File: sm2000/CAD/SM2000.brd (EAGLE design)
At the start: 160 x 100 mm, 228 parts, among them CN1 HDR100-3, CN10 ST-3509, CN11 HDR100-3, CN2 JS-MU3-002, CN3 DS-0518, CN5 ST-3509, CN8 ST-3509, J1 JMP-2PIN, J2 JMP-2PIN, J3 JMP-2PIN, J4 CONN-BOOM-XH-2A, P10 TPAD50, P11 TPAD50, P12 TPAD50, P13 TPAD50, P14 TPAD50, P16 TPAD50, P18 TPAD50, P19 TPAD50, P20 TPAD50, P21 TPAD50, P3 TPAD50, P4 TPAD50, P5 TPAD50, P6 TPAD50, P7 TPAD50, P8 TPAD50, P9 TPAD50, Q1 MMBT3904, Q2 MMBT3904, Q3 MMBT3904, Q4 MMBT3904, Q5 MMBT3904, Q6 MMBT3904, Q7 BC548, Q8 BC549, SW1 SW-LC2259, SW2 TS-026, SW3 SW-LC2259EENP, SW4 TS-026, SW5 TS-02B, U1 STM32F405VGT6, U10 DNL, U2 LD3985M33R, U3 STMPS2141, U4 EMIF02-USB03F2, U5 TPS54329E, U8 LM386M-1, U9 LMV341, X1 BU-SMA-H, X2 BU-SMA-H

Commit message: Continued edit of SM2000 .sch & .brd   RGB
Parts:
- removed R55: 0 Ohm, AA-ipc-7351-resistor:RESC1608X55N
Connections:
- removed net !CPPT!: U1.57
- removed net DAC1_OUT: R55.2
- removed net N$11: R55.1, U1.29
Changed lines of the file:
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@@
 <element name="C49" library="AA-ipc-7351-capacitor" package="CAPC1005X60N" value="100nF,25V" x="-72.39" y="129.54"/>
 <element name="FB7" library="_RoweTel" package="FE0805" value="FB0805" x="-54.61" y="120.65"/>
-<element name="R55" library="AA-ipc-7351-resistor" package="RESC1608X55N" value="0 Ohm" x="-123.19" y="95.25"/>
 <element name="R54" library="AA-ipc-7351-resistor" package="RESC1608X55N" value="0 Ohm" x="-116.84" y="95.25"/>
 <element name="C55" library="AA-ipc-7351-capacitor" package="CAPC1005X60N" value="1nF,25V,0402" x="-91.44" y="129.54"/>
@@
 <wire x1="-33.37" y1="3.68" x2="-27.17" y2="106.68" width="0" layer="19" extent="1-1"/>
 </signal>
-<signal name="!CPPT!">
-<contactref element="U1" pad="57"/>
-</signal>
 <signal name="!TEST!">
 <contactref element="R4" pad="2"/>
@@
 <wire x1="-97.79" y1="10" x2="-92.24" y2="95.25" width="0" layer="19" extent="1-1"/>
 </signal>
-<signal name="DAC1_OUT">
-<contactref element="R55" pad="2"/>
-</signal>
 <signal name="DAC2_OUT">
 <contactref element="R54" pad="2"/>
@@
 <wire x1="-105.41" y1="115.57" x2="-64.3" y2="95.25" width="0" layer="19" extent="1-1"/>
 <wire x1="-116.04" y1="95.25" x2="-105.41" y2="115.57" width="0" layer="19" extent="1-1"/>
-</signal>
-<signal name="N$11">
-<contactref element="R55" pad="1"/>
-<contactref element="U1" pad="29"/>
-<wire x1="-31.62" y1="6.93" x2="-123.99" y2="95.25" width="0" layer="19" extent="1-1"/>
 </signal>
 <signal name="N$13">
@@
 </signal>
 <signal name="N$90">
+<contactref element="C76" pad="2"/>
 <contactref element="C69" pad="1"/>
-<contactref element="C76" pad="2"/>
 <contactref element="X2" pad="1"/>
 <wire x1="-91.07" y1="88.9" x2="-118.11" y2="29.21" width="0" layer="19" extent="1-1"/>

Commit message: MERGE SCHEMATICS INTO sm2000.SCH AND UPDATE LIBRARY rgb
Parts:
- added C100, C93: 33p, rcl:C025-024X044
- added C118, C121, C124, C125, C126, C129, C131, C91, C92, C97: 0.1u, rcl:C025-024X044
- added C119: 10uF, _RoweTel:C1210
- added C120: 39pF, rcl:C025-024X044
- added C122, C89: 5p6, rcl:C025-024X044
- added C123: 2-12pF, c-trimm:3008
- added C127: 27pF, rcl:C025-024X044
- added C128, C132: 150pF, rcl:C025-024X044
- added C130, C133, C134, C88, C90, C96, C98: 1n, rcl:C025-024X044
- added C87: 22pF, AA-ipc-7351-capacitor:CAPC2012X145AN
- added C94: 22p, rcl:C025-024X044
- added C95: 1n DNL, rcl:C025-024X044
- added C99: 47p, rcl:C025-024X044
- added FB11, FB14, FB15, FB6: FB0805, _RoweTel:FE0805
- added L10: 168nH, rcl:0204/5
- added L11, L13: RFC, inductor-neosid:Z15/4
- added L12: 54nH, rcl:0204/5
- added L14, L15: 57nH air core 4T 2mm ID, rcl:0204/5
- added L20: 5.7uH +/- 10% Q>20, rcl:0204/5
- added L21: 9.2uH +/- 10% Q>20, rcl:0204/5
- added L22: 5.2uH +/- 10% Q>20, rcl:0204/5
- added L23: 15uH +/- 10% Q>20, rcl:0204/5
- added L9: 57nH, rcl:0204/5
- added Q12: BRF92, transistor:SOT23-EBC
- added Q13: BFQ19, transistor:SOT23-EBC
- added Q14: RD01MUS2, _RoweTel:SOT89
- added Q17, Q18: MMT2904, transistor:SOT23-EBC
- added R108, R60, R93: 3k, AA-ipc-7351-resistor:RESC2012X70N
- added R109, R113, R94: 1k, AA-ipc-7351-resistor:RESC2012X70N
- added R110, R96, R97: 10, AA-ipc-7351-resistor:RESC2012X70N
- added R111: 33k, AA-ipc-7351-resistor:RESC2012X70N
- added R112: 15k, AA-ipc-7351-resistor:RESC2012X70N
- added R114, R95: 50, AA-ipc-7351-resistor:RESC2012X70N
- added R115, R92: 150, AA-ipc-7351-resistor:RESC2012X70N
- added R55: 10k, AA-ipc-7351-resistor:RESC2012X70N
- added R98: 47 DNL, AA-ipc-7351-resistor:RESC2012X70N
- added R99: 4k7, AA-ipc-7351-resistor:RESC2012X70N
- added U$10, U$11: ECS-10.7-15B, _RoweTel:HC49/S
- added U7: SA612A, _RoweTel:SO-08
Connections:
- new net N$11: C100.1, L14.2
- new net N$112: C87.2, L9.1
- new net N$113: C95.1, R98.1
- new net N$114: C96.1, FB11.1, R99.2
- new net N$115: C97.1, FB6.2, R99.1
- new net N$116: L13.1
- new net N$118: C93.1, C98.2, L15.1
- new net N$140: C118.1, Q17.C, R108.2, R110.2, R111.2
- new net N$141: C121.2, Q17.B, Q18.C, R108.1
- new net N$142: C119.1, FB14.1, R110.1
- new net N$143: C120.1, L20.2, U$11.1
- new net N$144: C122.1, U$10.2, U$11.2
- new net N$145: C121.1, C123.+, L21.2, U$10.1
- new net N$146: C124.1, Q18.B, R111.1, R112.2
- new net N$147: C125.1, Q18.E, R113.2
- new net N$148: C126.1, Q17.E, R109.2
- new net N$149: C126.2, C127.1, C128.2, R114.2
- new net N$150: C128.1, C129.2, L22.2, U7.2
- new net N$151: C127.2, L22.1, U7.1
- new net N$152: FB15.2, R115.2
- new net N$153: C130.2, C131.2, R115.1, U7.8
- new net N$154: C132.2, U7.6
- new net N$155: C132.1
- new net N$156: C133.2, L23.1, U7.4
- new net N$157: C134.2, L23.2
- new net N$32: C98.1, L11.1, Q14.3
- new net N$33: C94.1, FB11.2, Q14.1, R98.2
- new net N$70: C88.1, Q12.E, R92.2
- new net N$71: C90.1, Q13.E, R95.2
- new net N$73: C91.1, L10.1, R55.2, R96.2
- new net N$74: C92.1, L12.1, R93.2, R96.1, R97.2
- new net N$75: C89.1, Q13.B, R93.1, R94.2
- new net N$78: C87.1, Q12.B, R55.1, R60.2
- new net N$79: L11.2, L13.2, R97.1
- new net N$82: C89.2, L10.2, Q12.C
- new net N$84: C94.2, L12.2, Q13.C
- new net N$9: C99.1, L14.1, L15.2
- new net VGG: FB6.1
- net +12V: now also FB14.2, FB15.1
- net GND: now also C100.2, C118.2, C119.2, C120.2, C122.2, C123.-, C129.1, C131.1, C133.1, C134.1, C88.2, C90.2, C91.2, C92.2, C93.2, C95.2, C96.2, C97.2, C99.2, L21.1, L9.2, Q14.2, Q14.2.1, R109.1, R113.1, R114.1, R60.1, R92.1, R94.1, R95.1, U7.3

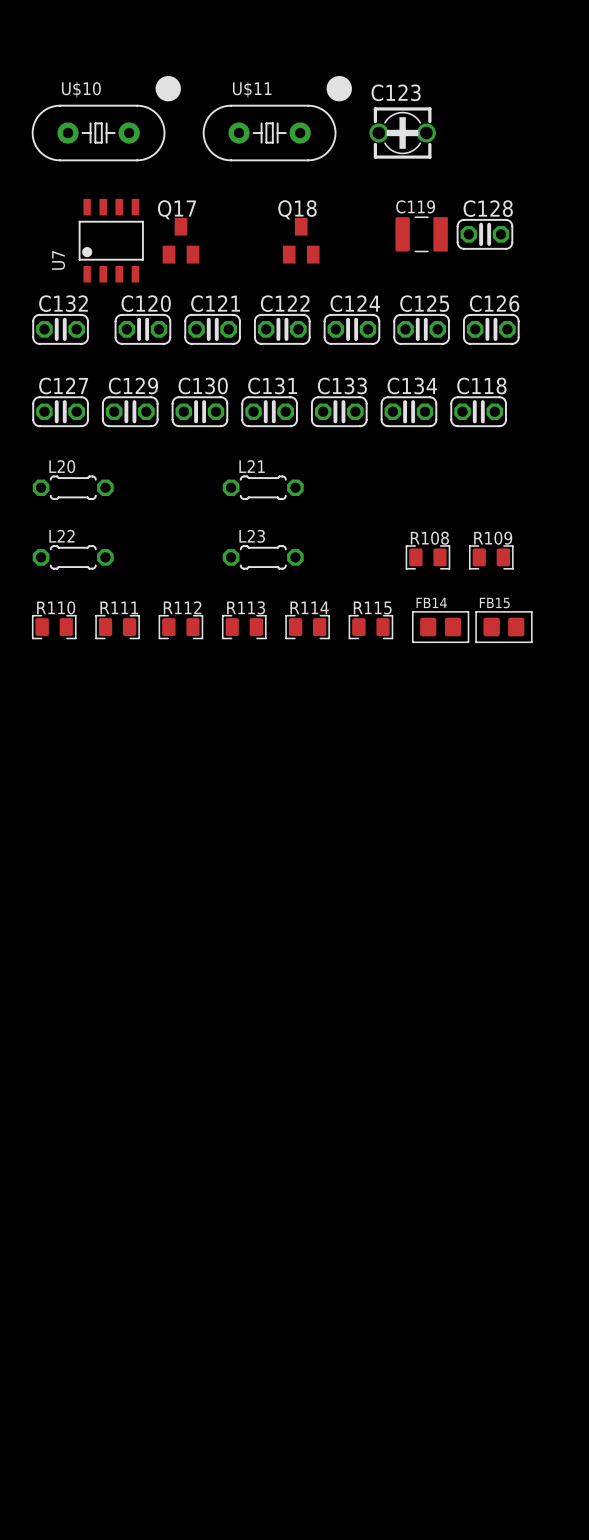
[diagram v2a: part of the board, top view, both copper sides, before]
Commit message: INTEGRATED 1ST MIXER BPF SWITCH INTO SM2000.SCH. CORRECTED CENTERING ON SOME COMPONENTS IN ROWETEL.LBR SHORTENED LEADS ON FB0805 SYMBOL. RGB
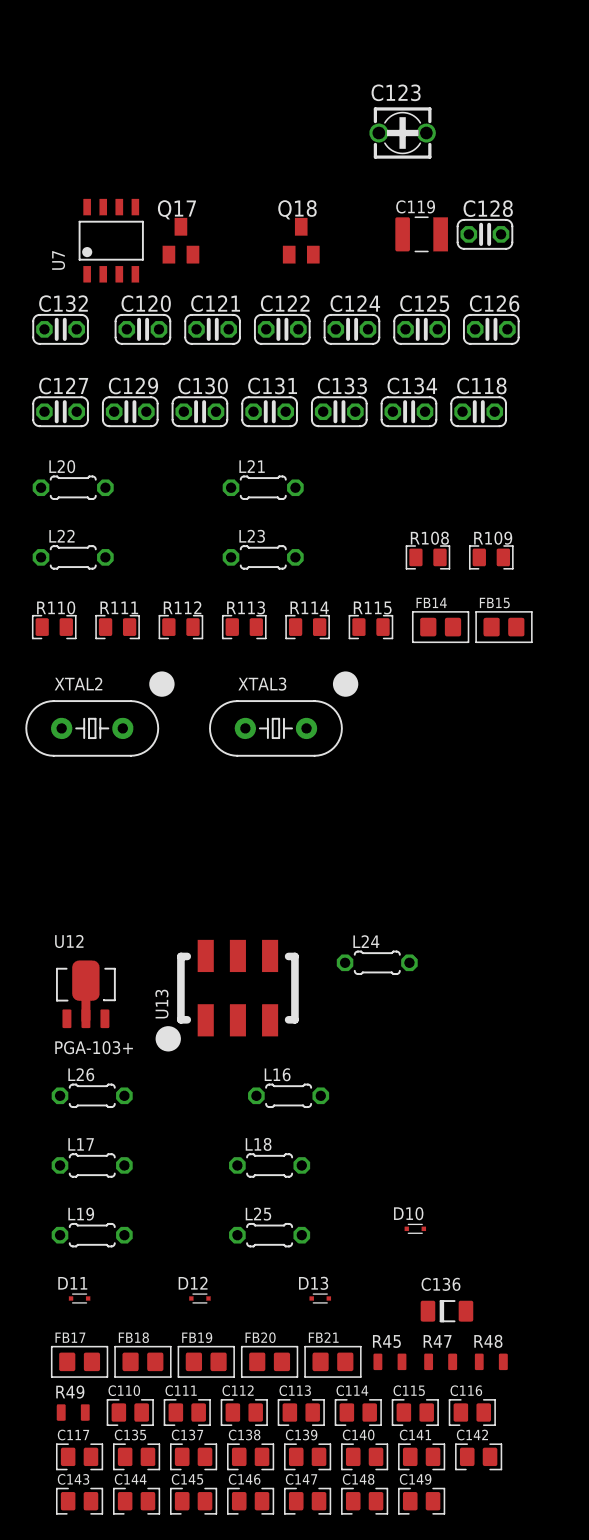
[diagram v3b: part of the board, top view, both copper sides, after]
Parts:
- removed U$10, U$11: ECS-10.7-15B, _RoweTel:HC49/S
- added C110, C113, C138, C141: 12p, AA-ipc-7351-capacitor:CAPC2012X145AN
- added C111, C112, C139, C140: 3p3, AA-ipc-7351-capacitor:CAPC2012X145AN
- added C114, C142: 0.5p, AA-ipc-7351-capacitor:CAPC2012X145AN
- added C115, C116, C117, C135, C137, C147, C148, C149: 1n, AA-ipc-7351-capacitor:CAPC2012X145AN
- added C136: 1u, _RoweTel:C1206-TANT
- added C143, C144: 2p2, AA-ipc-7351-capacitor:CAPC2012X145AN
- added C145, C146: 22p, AA-ipc-7351-capacitor:CAPC2012X145AN
- added D10, D11, D12, D13: BAR64-02V, _RoweTel:SC79_INFINEON
- added FB17, FB18, FB19, FB20, FB21: FB0805, _RoweTel:FE0805
- added L16, L17, L18, L19: 68nH 4.5T 5mm ID, rcl:0204/5
- added L24: 260nH 8T 6.25mm ID, rcl:0204/5
- added L25: 53nH 3T 5mm ID, rcl:0204/5
- added L26: 220nH 7T 6.25mm ID, rcl:0204/5
- added R45, R47: 18k, _RoweTel:RR0805
- added R48: 68k, _RoweTel:RR0805
- added R49: 2k2, _RoweTel:RR0805
- added U12: PGA-103+, _RoweTel:DF782
- added U13: ADE-1, _RoweTel:ADE-1
- added XTAL2, XTAL3: ECS-10.7-15B, _RoweTel:HC49/S
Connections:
- net N$157 renamed BBAMP
- new net N$125: C110.1, C111.1, C114.2, L16.1
- new net N$126: C112.2, C113.2, C114.1, L17.1
- new net N$127: C111.2, U13.3
- new net N$128: C116.1, FB19.2, R45.2
- new net N$129: C115.1, FB18.1, R47.2
- new net N$130: C117.1, D10.A, FB19.1
- new net N$131: C117.2, FB20.1, U12.3
- new net N$132: C135.1, C136.1, FB20.2, FB21.1
- new net N$133: FB21.2
- new net N$134: C137.1, D11.A, FB18.2
- new net N$135: C112.1, D10.C, D11.C, FB17.2
- new net N$136: C138.1, C139.1, C142.2, L18.1
- new net N$137: C140.2, C141.2, C142.1, L19.1
- new net N$138: C139.2
- new net N$139: C143.1, C144.2, L24.1
- new net N$149: C140.1, C145.1, D12.A, L25.1
- new net N$157: C149.1, D13.A, L26.2
- new net N$158: C148.1, L26.1, R49.1
- new net N$50: U7.2
- new net N$51: C128.1, C129.2, L22.2
- new net TX2NDLO: C125.2, C132.1
- new net TXDAC: C124.2
- net GND: now also C110.2, C113.1, C115.2, C116.2, C130.1, C135.2, C136.2, C138.2, C141.1, C145.2, C146.2, C148.2, D12.C, FB17.1, L16.2, L17.2, L18.2, L19.2, L24.2, R112.1, R48.1, U12.2, U12.4
- net N$143: now also XTAL2.1; no longer U$11.1
- net N$144: now also XTAL2.2, XTAL3.1; no longer U$10.2, U$11.2
- net N$145: now also XTAL3.2; no longer U$10.1
- net N$150: now also C146.1, C147.2, D13.C, L25.2; no longer C128.1, C129.2, L22.2, U7.2
- net N$155: now also C147.1, R48.2; no longer C132.1
